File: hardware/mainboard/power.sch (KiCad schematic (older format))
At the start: 13 parts, among them U1 LM4040DBZ-10, U2 LM1117-3.3

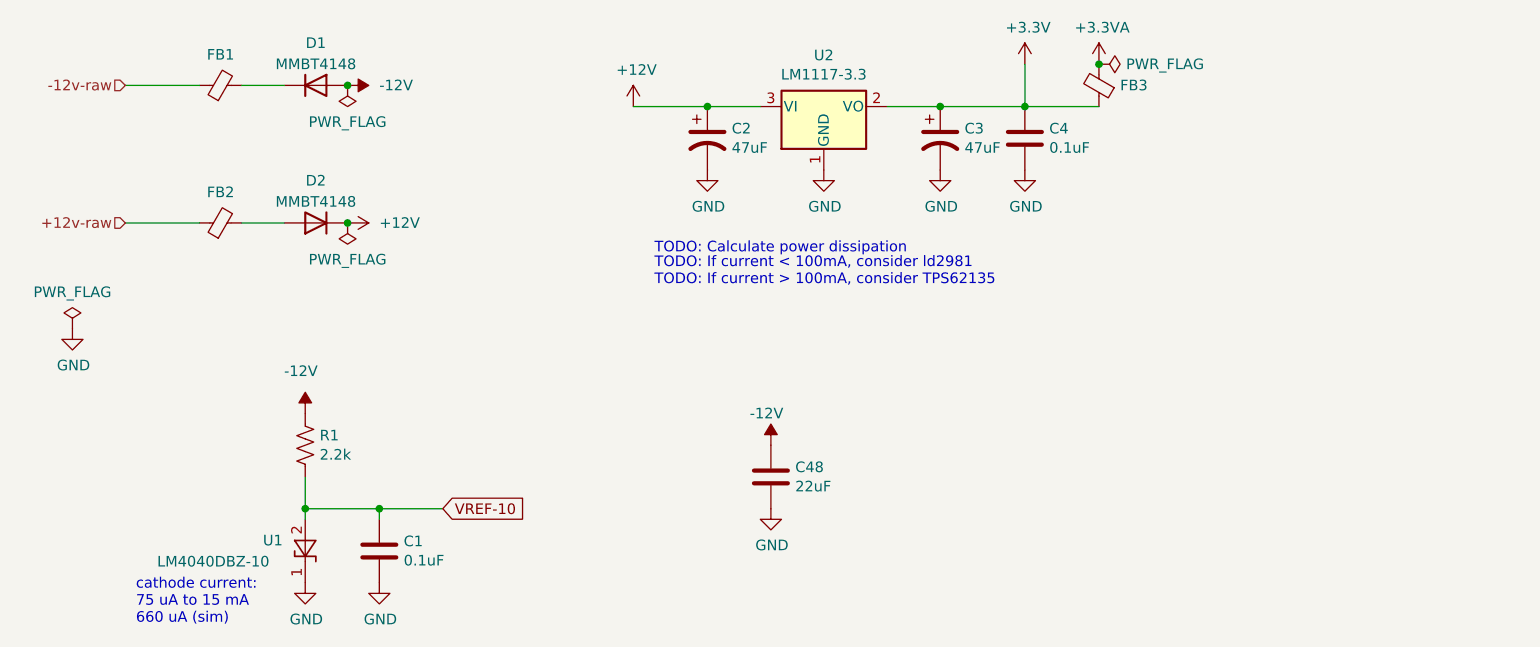
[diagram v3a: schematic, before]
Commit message: Cleanup some comments in the schematic
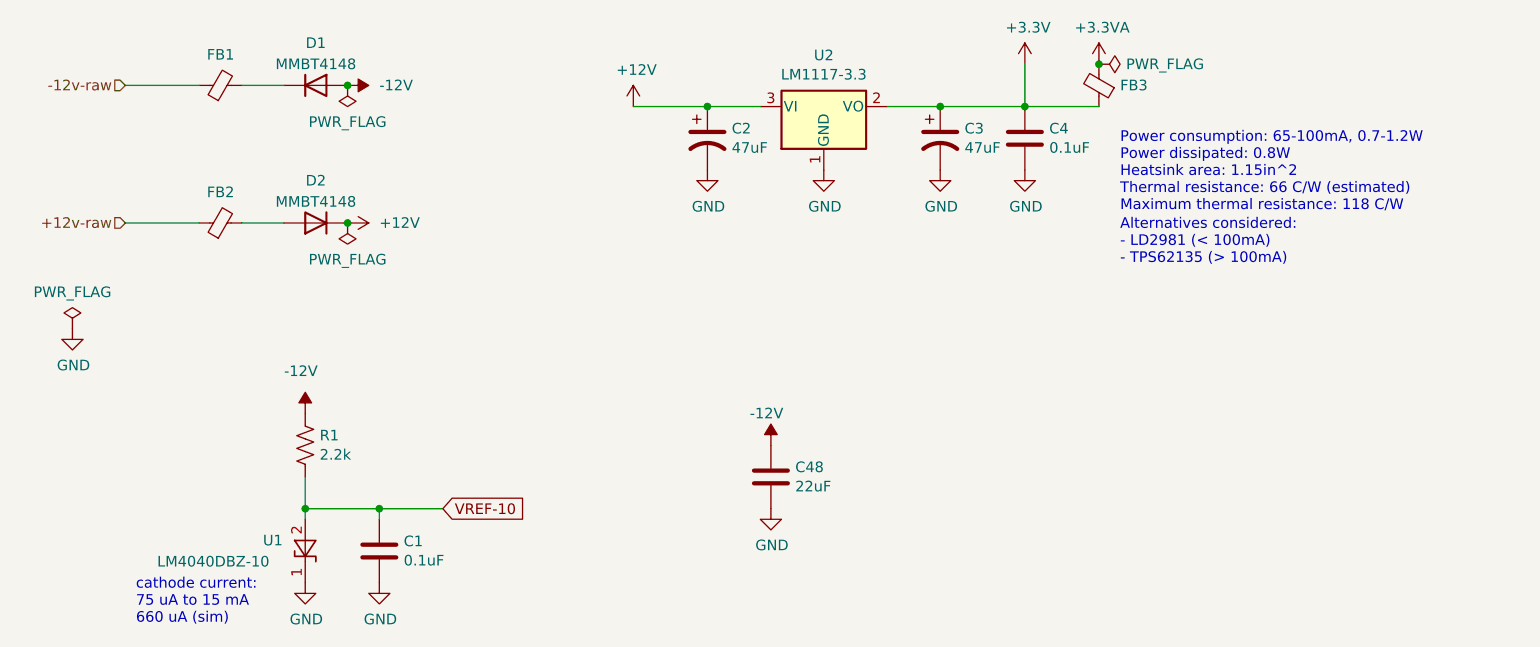
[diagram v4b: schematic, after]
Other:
- note added: "Alternatives considered:\n- LD2981 (< 100mA)\n- TPS62135 (> 100mA)"
- note added: "Power consumption: 65-100mA, 0.7-1.2W\nPower dissipated: 0.8W\nHeatsink area: 1.15in^2\nThermal resistance: 66 C/W (estimated)\nMaximum thermal resistance: 118 C/W\n"
- note removed: "TODO: Calculate power dissipation"
- note removed: "TODO: If current < 100mA, consider ld2981\nTODO: If current > 100mA, consider TPS62135"
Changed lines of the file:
@@
 Wire Wire Line
 	1900 1750 2100 1750
-Text Notes 3850 1900 0    50   ~ 0
-TODO: Calculate power dissipation
+Text Notes 6050 1700 0    50   ~ 0
+Power consumption: 65-100mA, 0.7-1.2W\nPower dissipated: 0.8W\nHeatsink area: 1.15in^2\nThermal resistance: 66 C/W (estimated)\nMaximum thermal resistance: 118 C/W\n
 $Comp
 L Reference_Voltage:LM4040DBZ-10 U1
@@
 Wire Wire Line
 	1350 1100 1700 1100
-Text Notes 3850 2050 0    50   ~ 0
-TODO: If current < 100mA, consider ld2981\nTODO: If current > 100mA, consider TPS62135
+Text Notes 6050 1950 0    50   ~ 0
+Alternatives considered:\n- LD2981 (< 100mA)\n- TPS62135 (> 100mA)
 $Comp
 L power:GND #PWR02

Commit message: hardware: finalize v3 of mainboard for production
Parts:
- C1, C4: Reqs (none) -> bypass
- C48: Reqs (none) -> power bypass; mpn GRM21BR61E226ME44K -> CL21A226MAQNNNE; mpn alt (none) -> GRM21BR61E226ME44L
- R1: Reqs 1% -> 1%, vref current control
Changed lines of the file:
@@
 Sheet 2 7
 Title "Castor & Pollux"
-Date "2021-02-01"
+Date "2021-02-05"
 Rev "v3"
 Comp "Winterbloom"
@@
 F 6 "10%, 25v" H 5600 1350 50  0001 C CNN "mpn specs"
 F 7 "GCM188R91E104KA37D" H 5600 1350 50  0001 C CNN "mpn alt"
+F 8 "bypass" H 5600 1350 50  0001 C CNN "Reqs"
 	1    5600 1350
 	1    0    0    -1
@@
 F 4 "yes" H 2200 2800 50  0001 C CNN "finalized"
 F 5 "ERA-3AED222V" H 2200 2800 50  0001 C CNN "mpn"
-F 6 "1%" H 2200 2800 50  0001 C CNN "Reqs"
+F 6 "1%, vref current control" H 2200 2800 50  0001 C CNN "Reqs"
 F 7 "100mW" H 2200 2800 50  0001 C CNN "mpn specs"
 	1    2200 2800
@@
 F 6 "10%, 25v" H 2550 3300 50  0001 C CNN "mpn specs"
 F 7 "GCM188R91E104KA37D" H 2550 3300 50  0001 C CNN "mpn alt"
+F 8 "bypass" H 2550 3300 50  0001 C CNN "Reqs"
 	1    2550 3300
 	1    0    0    -1
@@
 F 2 "Capacitor_SMD:C_0805_2012Metric_Pad1.15x1.40mm_HandSolder" H 4438 2800 50  0001 C CNN
 F 3 "~" H 4400 2950 50  0001 C CNN
-F 4 "GRM21BR61E226ME44K" H 4400 2950 50  0001 C CNN "mpn"
+F 4 "CL21A226MAQNNNE" H 4400 2950 50  0001 C CNN "mpn"
 F 5 "yes" H 4400 2950 50  0001 C CNN "finalized"
 F 6 "20% 25v" H 4400 2950 50  0001 C CNN "mpn specs"
+F 7 "power bypass" H 4400 2950 50  0001 C CNN "Reqs"
+F 8 "GRM21BR61E226ME44L" H 4400 2950 50  0001 C CNN "mpn alt"
 	1    4400 2950
 	1    0    0    -1

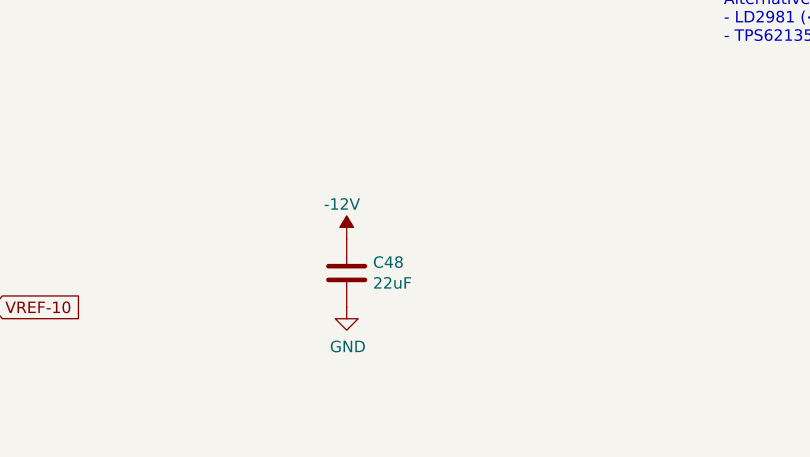
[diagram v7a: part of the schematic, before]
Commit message: hardware: finish up mpn assignments for mainboard
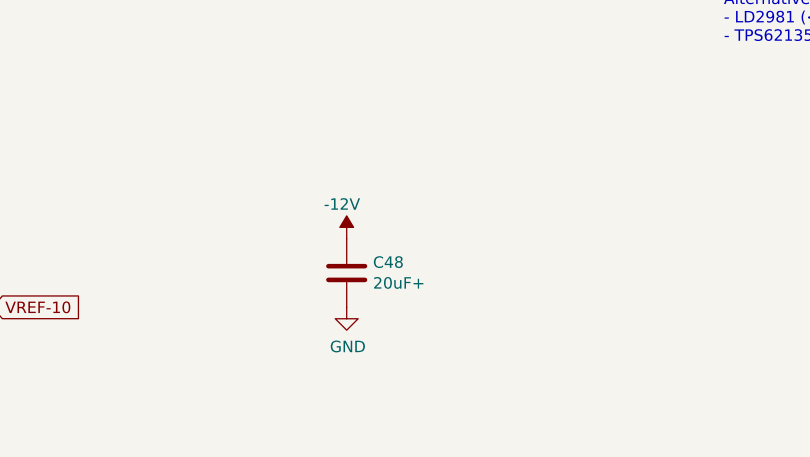
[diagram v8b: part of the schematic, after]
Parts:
- C48: value 22uF -> 20uF+; Reqs power bypass -> power bypass, 25v; mpn CL21A226MAQNNNE -> CL21A226MAQNNN; mpn specs 20% 25v -> 22uF 20% 25v
- R1: Reqs 1%, vref current control -> 1%, 60mW, vref current control; mpn ERA-3AED222V -> MCT06030C2201FP500; mpn specs 100mW -> 125mW, 1%
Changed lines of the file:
@@
 F 3 "~" H 2200 2800 50  0001 C CNN
 F 4 "yes" H 2200 2800 50  0001 C CNN "finalized"
-F 5 "ERA-3AED222V" H 2200 2800 50  0001 C CNN "mpn"
-F 6 "1%, vref current control" H 2200 2800 50  0001 C CNN "Reqs"
-F 7 "100mW" H 2200 2800 50  0001 C CNN "mpn specs"
+F 5 "MCT06030C2201FP500" H 2200 2800 50  0001 C CNN "mpn"
+F 6 "1%, 60mW, vref current control" H 2200 2800 50  0001 C CNN "Reqs"
+F 7 "125mW,  1%" H 2200 2800 50  0001 C CNN "mpn specs"
 	1    2200 2800
 	1    0    0    -1
@@
 P 4400 2950
 F 0 "C48" H 4515 2996 50  0000 L CNN
-F 1 "22uF" H 4515 2905 50  0000 L CNN
+F 1 "20uF+" H 4515 2905 50  0000 L CNN
 F 2 "Capacitor_SMD:C_0805_2012Metric_Pad1.15x1.40mm_HandSolder" H 4438 2800 50  0001 C CNN
 F 3 "~" H 4400 2950 50  0001 C CNN
-F 4 "CL21A226MAQNNNE" H 4400 2950 50  0001 C CNN "mpn"
+F 4 "CL21A226MAQNNN" H 4400 2950 50  0001 C CNN "mpn"
 F 5 "yes" H 4400 2950 50  0001 C CNN "finalized"
-F 6 "20% 25v" H 4400 2950 50  0001 C CNN "mpn specs"
-F 7 "power bypass" H 4400 2950 50  0001 C CNN "Reqs"
+F 6 "22uF 20% 25v" H 4400 2950 50  0001 C CNN "mpn specs"
+F 7 "power bypass, 25v" H 4400 2950 50  0001 C CNN "Reqs"
 F 8 "GRM21BR61E226ME44L" H 4400 2950 50  0001 C CNN "mpn alt"
 	1    4400 2950
